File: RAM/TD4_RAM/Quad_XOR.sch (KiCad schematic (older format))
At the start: 2 parts, among them U2 74HC86

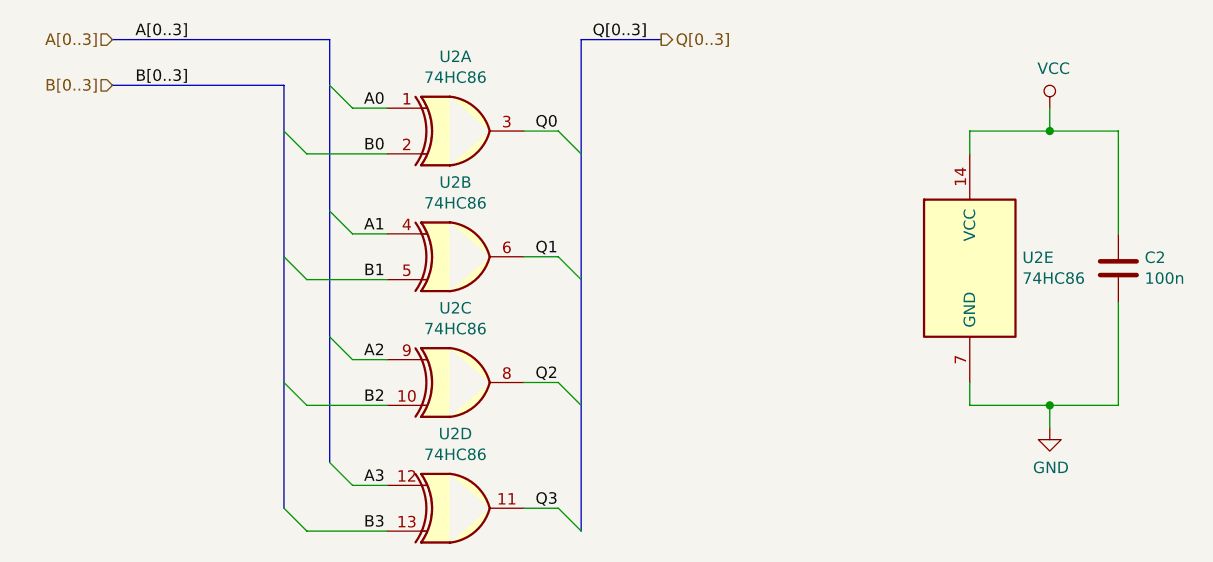
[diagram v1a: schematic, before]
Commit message: Main RAM blocks routed
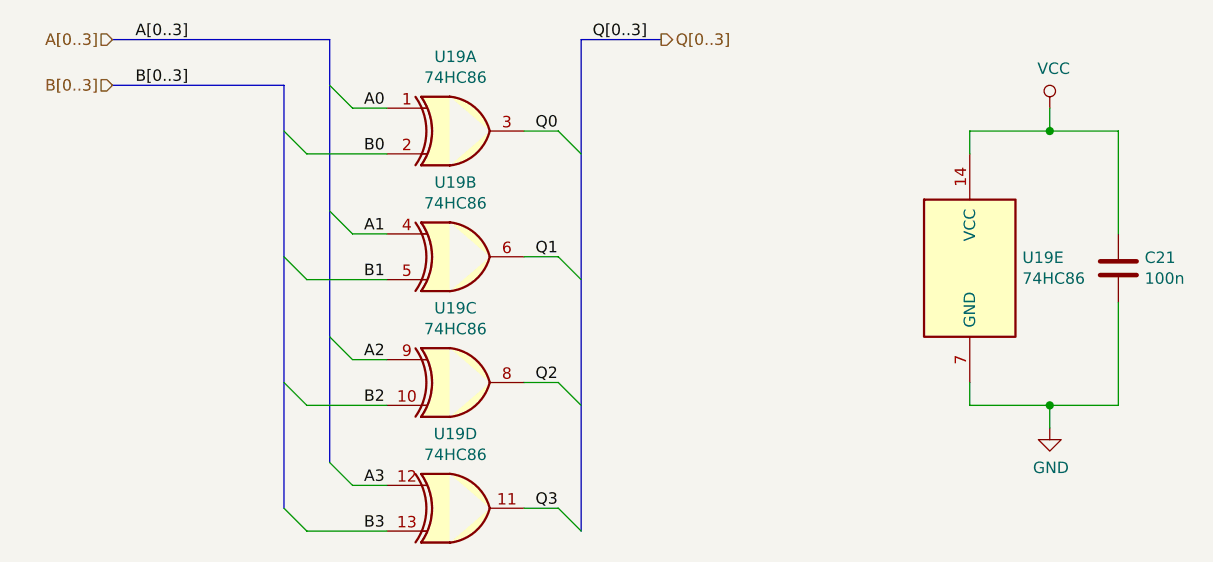
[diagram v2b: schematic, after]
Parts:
- renumbered C2 to C4
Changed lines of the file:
@@
 AR Path="/5C5DC05E/5CCDF31F/5C5DC2EE" Ref="U18"  Part="1"
 AR Path="/5C5DC05E/5CCE6007/5C5DC2EE" Ref="U19"  Part="1"
-F 0 "U2" H 4850 2925 50  0000 C CNN
+F 0 "U19" H 4850 2925 50  0000 C CNN
 F 1 "74HC86" H 4850 2834 50  0000 C CNN
 F 2 "Package_SO:SOIC-14_3.9x8.7mm_P1.27mm" H 4850 2600 50  0001 C CNN
@@
 AR Path="/5C5DC05E/5CCDF31F/5C5DC376" Ref="U18"  Part="2"
 AR Path="/5C5DC05E/5CCE6007/5C5DC376" Ref="U19"  Part="2"
-F 0 "U2" H 4850 3475 50  0000 C CNN
+F 0 "U19" H 4850 3475 50  0000 C CNN
 F 1 "74HC86" H 4850 3384 50  0000 C CNN
 F 2 "Package_SO:SOIC-14_3.9x8.7mm_P1.27mm" H 4850 3150 50  0001 C CNN
@@
 AR Path="/5C5DC05E/5CCDF31F/5C5DC396" Ref="U18"  Part="3"
 AR Path="/5C5DC05E/5CCE6007/5C5DC396" Ref="U19"  Part="3"
-F 0 "U2" H 4850 4025 50  0000 C CNN
+F 0 "U19" H 4850 4025 50  0000 C CNN
 F 1 "74HC86" H 4850 3934 50  0000 C CNN
 F 2 "Package_SO:SOIC-14_3.9x8.7mm_P1.27mm" H 4850 3700 50  0001 C CNN
@@
 AR Path="/5C5DC05E/5CCDF31F/5C5DC3D2" Ref="U18"  Part="4"
 AR Path="/5C5DC05E/5CCE6007/5C5DC3D2" Ref="U19"  Part="4"
-F 0 "U2" H 4850 4575 50  0000 C CNN
+F 0 "U19" H 4850 4575 50  0000 C CNN
 F 1 "74HC86" H 4850 4484 50  0000 C CNN
 F 2 "Package_SO:SOIC-14_3.9x8.7mm_P1.27mm" H 4850 4250 50  0001 C CNN
@@
 AR Path="/5C5DC05E/5CCDF31F/5C5DC430" Ref="U18"  Part="5"
 AR Path="/5C5DC05E/5CCE6007/5C5DC430" Ref="U19"  Part="5"
-F 0 "U2" H 7330 3246 50  0000 L CNN
+F 0 "U19" H 7330 3246 50  0000 L CNN
 F 1 "74HC86" H 7330 3155 50  0000 L CNN
 F 2 "Package_SO:SOIC-14_3.9x8.7mm_P1.27mm" H 7100 3200 50  0001 C CNN
@@
 $EndComp
 $Comp
-L Device:C C2
+L Device:C C4
 U 1 1 5C5DC564
 P 7750 3200
-AR Path="/5C5DC05E/5C5DC213/5C5DC564" Ref="C2"  Part="1"
+AR Path="/5C5DC05E/5C5DC213/5C5DC564" Ref="C4"  Part="1"
 AR Path="/5C5DC05E/5C5E95C7/5C5DC564" Ref="C?"  Part="1"
 AR Path="/5C5DC05E/5C5E965E/5C5DC564" Ref="C?"  Part="1"
@@
 AR Path="/5C5DC05E/5C8E6B2E/5C5DC564" Ref="C?"  Part="1"
 AR Path="/5C5DC05E/5C8E6B33/5C5DC564" Ref="C?"  Part="1"
-AR Path="/5C5DC05E/5CC7FE6F/5C5DC564" Ref="C5"  Part="1"
-AR Path="/5C5DC05E/5CC86B57/5C5DC564" Ref="C6"  Part="1"
-AR Path="/5C5DC05E/5CC8D83F/5C5DC564" Ref="C7"  Part="1"
-AR Path="/5C5DC05E/5CC94527/5C5DC564" Ref="C8"  Part="1"
-AR Path="/5C5DC05E/5CC9B20F/5C5DC564" Ref="C9"  Part="1"
-AR Path="/5C5DC05E/5CCA1EF7/5C5DC564" Ref="C10"  Part="1"
-AR Path="/5C5DC05E/5CCA8BDF/5C5DC564" Ref="C11"  Part="1"
-AR Path="/5C5DC05E/5CCAF8C7/5C5DC564" Ref="C12"  Part="1"
-AR Path="/5C5DC05E/5CCB65AF/5C5DC564" Ref="C13"  Part="1"
-AR Path="/5C5DC05E/5CCBD297/5C5DC564" Ref="C14"  Part="1"
-AR Path="/5C5DC05E/5CCC3F7F/5C5DC564" Ref="C15"  Part="1"
-AR Path="/5C5DC05E/5CCCAC67/5C5DC564" Ref="C16"  Part="1"
+AR Path="/5C5DC05E/5CC7FE6F/5C5DC564" Ref="C7"  Part="1"
+AR Path="/5C5DC05E/5CC86B57/5C5DC564" Ref="C8"  Part="1"
+AR Path="/5C5DC05E/5CC8D83F/5C5DC564" Ref="C9"  Part="1"
+AR Path="/5C5DC05E/5CC94527/5C5DC564" Ref="C10"  Part="1"
+AR Path="/5C5DC05E/5CC9B20F/5C5DC564" Ref="C11"  Part="1"
+AR Path="/5C5DC05E/5CCA1EF7/5C5DC564" Ref="C12"  Part="1"
+AR Path="/5C5DC05E/5CCA8BDF/5C5DC564" Ref="C13"  Part="1"
+AR Path="/5C5DC05E/5CCAF8C7/5C5DC564" Ref="C14"  Part="1"
+AR Path="/5C5DC05E/5CCB65AF/5C5DC564" Ref="C15"  Part="1"
+AR Path="/5C5DC05E/5CCBD297/5C5DC564" Ref="C16"  Part="1"
+AR Path="/5C5DC05E/5CCC3F7F/5C5DC564" Ref="C17"  Part="1"
+AR Path="/5C5DC05E/5CCCAC67/5C5DC564" Ref="C18"  Part="1"
 AR Path="/5C5DC05E/5CCD194F/5C5DC564" Ref="C?"  Part="1"
-AR Path="/5C5DC05E/5CCD8637/5C5DC564" Ref="C17"  Part="1"
-AR Path="/5C5DC05E/5CCDF31F/5C5DC564" Ref="C18"  Part="1"
-AR Path="/5C5DC05E/5CCE6007/5C5DC564" Ref="C19"  Part="1"
-F 0 "C2" H 7865 3246 50  0000 L CNN
+AR Path="/5C5DC05E/5CCD8637/5C5DC564" Ref="C19"  Part="1"
+AR Path="/5C5DC05E/5CCDF31F/5C5DC564" Ref="C20"  Part="1"
+AR Path="/5C5DC05E/5CCE6007/5C5DC564" Ref="C21"  Part="1"
+F 0 "C21" H 7865 3246 50  0000 L CNN
 F 1 "100n" H 7865 3155 50  0000 L CNN
 F 2 "Capacitor_SMD:C_0805_2012Metric" H 7788 3050 50  0001 C CNN
@@
 Q[0..3]
 $Comp
-L power:GND #PWR019
+L power:GND #PWR024
 U 1 1 5C5DF5EB
 P 7450 3900
-AR Path="/5C5DC05E/5C5DC213/5C5DF5EB" Ref="#PWR019"  Part="1"
+AR Path="/5C5DC05E/5C5DC213/5C5DF5EB" Ref="#PWR024"  Part="1"
 AR Path="/5C5DC05E/5C5E95C7/5C5DF5EB" Ref="#PWR?"  Part="1"
 AR Path="/5C5DC05E/5C5E965E/5C5DF5EB" Ref="#PWR?"  Part="1"
@@
 AR Path="/5C5DC05E/5C8E6B2E/5C5DF5EB" Ref="#PWR?"  Part="1"
 AR Path="/5C5DC05E/5C8E6B33/5C5DF5EB" Ref="#PWR?"  Part="1"
-AR Path="/5C5DC05E/5CC7FE6F/5C5DF5EB" Ref="#PWR057"  Part="1"
-AR Path="/5C5DC05E/5CC86B57/5C5DF5EB" Ref="#PWR059"  Part="1"
-AR Path="/5C5DC05E/5CC8D83F/5C5DF5EB" Ref="#PWR061"  Part="1"
-AR Path="/5C5DC05E/5CC94527/5C5DF5EB" Ref="#PWR063"  Part="1"
-AR Path="/5C5DC05E/5CC9B20F/5C5DF5EB" Ref="#PWR065"  Part="1"
-AR Path="/5C5DC05E/5CCA1EF7/5C5DF5EB" Ref="#PWR067"  Part="1"
-AR Path="/5C5DC05E/5CCA8BDF/5C5DF5EB" Ref="#PWR069"  Part="1"
-AR Path="/5C5DC05E/5CCAF8C7/5C5DF5EB" Ref="#PWR071"  Part="1"
-AR Path="/5C5DC05E/5CCB65AF/5C5DF5EB" Ref="#PWR073"  Part="1"
-AR Path="/5C5DC05E/5CCBD297/5C5DF5EB" Ref="#PWR075"  Part="1"
-AR Path="/5C5DC05E/5CCC3F7F/5C5DF5EB" Ref="#PWR077"  Part="1"
-AR Path="/5C5DC05E/5CCCAC67/5C5DF5EB" Ref="#PWR079"  Part="1"
+AR Path="/5C5DC05E/5CC7FE6F/5C5DF5EB" Ref="#PWR062"  Part="1"
+AR Path="/5C5DC05E/5CC86B57/5C5DF5EB" Ref="#PWR064"  Part="1"
+AR Path="/5C5DC05E/5CC8D83F/5C5DF5EB" Ref="#PWR066"  Part="1"
+AR Path="/5C5DC05E/5CC94527/5C5DF5EB" Ref="#PWR068"  Part="1"
+AR Path="/5C5DC05E/5CC9B20F/5C5DF5EB" Ref="#PWR070"  Part="1"
+AR Path="/5C5DC05E/5CCA1EF7/5C5DF5EB" Ref="#PWR072"  Part="1"
+AR Path="/5C5DC05E/5CCA8BDF/5C5DF5EB" Ref="#PWR074"  Part="1"
+AR Path="/5C5DC05E/5CCAF8C7/5C5DF5EB" Ref="#PWR076"  Part="1"
+AR Path="/5C5DC05E/5CCB65AF/5C5DF5EB" Ref="#PWR078"  Part="1"
+AR Path="/5C5DC05E/5CCBD297/5C5DF5EB" Ref="#PWR080"  Part="1"
+AR Path="/5C5DC05E/5CCC3F7F/5C5DF5EB" Ref="#PWR082"  Part="1"
+AR Path="/5C5DC05E/5CCCAC67/5C5DF5EB" Ref="#PWR084"  Part="1"
 AR Path="/5C5DC05E/5CCD194F/5C5DF5EB" Ref="#PWR?"  Part="1"
-AR Path="/5C5DC05E/5CCD8637/5C5DF5EB" Ref="#PWR081"  Part="1"
-AR Path="/5C5DC05E/5CCDF31F/5C5DF5EB" Ref="#PWR083"  Part="1"
-AR Path="/5C5DC05E/5CCE6007/5C5DF5EB" Ref="#PWR085"  Part="1"
-F 0 "#PWR019" H 7450 3650 50  0001 C CNN
+AR Path="/5C5DC05E/5CCD8637/5C5DF5EB" Ref="#PWR086"  Part="1"
+AR Path="/5C5DC05E/5CCDF31F/5C5DF5EB" Ref="#PWR088"  Part="1"
+AR Path="/5C5DC05E/5CCE6007/5C5DF5EB" Ref="#PWR090"  Part="1"
+F 0 "#PWR090" H 7450 3650 50  0001 C CNN
 F 1 "GND" H 7455 3727 50  0000 C CNN
 F 2 "" H 7450 3900 50  0001 C CNN
@@
 	7100 2600 7450 2600
 $Comp
-L power:VCC #PWR018
+L power:VCC #PWR023
 U 1 1 5C5E1083
 P 7450 2500
-AR Path="/5C5DC05E/5C5DC213/5C5E1083" Ref="#PWR018"  Part="1"
+AR Path="/5C5DC05E/5C5DC213/5C5E1083" Ref="#PWR023"  Part="1"
 AR Path="/5C5DC05E/5C5E95C7/5C5E1083" Ref="#PWR?"  Part="1"
 AR Path="/5C5DC05E/5C5E965E/5C5E1083" Ref="#PWR?"  Part="1"
@@
 AR Path="/5C5DC05E/5C8E6B2E/5C5E1083" Ref="#PWR?"  Part="1"
 AR Path="/5C5DC05E/5C8E6B33/5C5E1083" Ref="#PWR?"  Part="1"
-AR Path="/5C5DC05E/5CC7FE6F/5C5E1083" Ref="#PWR056"  Part="1"
-AR Path="/5C5DC05E/5CC86B57/5C5E1083" Ref="#PWR058"  Part="1"
-AR Path="/5C5DC05E/5CC8D83F/5C5E1083" Ref="#PWR060"  Part="1"
-AR Path="/5C5DC05E/5CC94527/5C5E1083" Ref="#PWR062"  Part="1"
-AR Path="/5C5DC05E/5CC9B20F/5C5E1083" Ref="#PWR064"  Part="1"
-AR Path="/5C5DC05E/5CCA1EF7/5C5E1083" Ref="#PWR066"  Part="1"
-AR Path="/5C5DC05E/5CCA8BDF/5C5E1083" Ref="#PWR068"  Part="1"
-AR Path="/5C5DC05E/5CCAF8C7/5C5E1083" Ref="#PWR070"  Part="1"
-AR Path="/5C5DC05E/5CCB65AF/5C5E1083" Ref="#PWR072"  Part="1"
-AR Path="/5C5DC05E/5CCBD297/5C5E1083" Ref="#PWR074"  Part="1"
-AR Path="/5C5DC05E/5CCC3F7F/5C5E1083" Ref="#PWR076"  Part="1"
-AR Path="/5C5DC05E/5CCCAC67/5C5E1083" Ref="#PWR078"  Part="1"
+AR Path="/5C5DC05E/5CC7FE6F/5C5E1083" Ref="#PWR061"  Part="1"
+AR Path="/5C5DC05E/5CC86B57/5C5E1083" Ref="#PWR063"  Part="1"
+AR Path="/5C5DC05E/5CC8D83F/5C5E1083" Ref="#PWR065"  Part="1"
+AR Path="/5C5DC05E/5CC94527/5C5E1083" Ref="#PWR067"  Part="1"
+AR Path="/5C5DC05E/5CC9B20F/5C5E1083" Ref="#PWR069"  Part="1"
+AR Path="/5C5DC05E/5CCA1EF7/5C5E1083" Ref="#PWR071"  Part="1"
+AR Path="/5C5DC05E/5CCA8BDF/5C5E1083" Ref="#PWR073"  Part="1"
+AR Path="/5C5DC05E/5CCAF8C7/5C5E1083" Ref="#PWR075"  Part="1"
+AR Path="/5C5DC05E/5CCB65AF/5C5E1083" Ref="#PWR077"  Part="1"
+AR Path="/5C5DC05E/5CCBD297/5C5E1083" Ref="#PWR079"  Part="1"
+AR Path="/5C5DC05E/5CCC3F7F/5C5E1083" Ref="#PWR081"  Part="1"
+AR Path="/5C5DC05E/5CCCAC67/5C5E1083" Ref="#PWR083"  Part="1"
 AR Path="/5C5DC05E/5CCD194F/5C5E1083" Ref="#PWR?"  Part="1"
-AR Path="/5C5DC05E/5CCD8637/5C5E1083" Ref="#PWR080"  Part="1"
-AR Path="/5C5DC05E/5CCDF31F/5C5E1083" Ref="#PWR082"  Part="1"
-AR Path="/5C5DC05E/5CCE6007/5C5E1083" Ref="#PWR084"  Part="1"
-F 0 "#PWR018" H 7450 2350 50  0001 C CNN
+AR Path="/5C5DC05E/5CCD8637/5C5E1083" Ref="#PWR085"  Part="1"
+AR Path="/5C5DC05E/5CCDF31F/5C5E1083" Ref="#PWR087"  Part="1"
+AR Path="/5C5DC05E/5CCE6007/5C5E1083" Ref="#PWR089"  Part="1"
+F 0 "#PWR089" H 7450 2350 50  0001 C CNN
 F 1 "VCC" H 7467 2673 50  0000 C CNN
 F 2 "" H 7450 2500 50  0001 C CNN
